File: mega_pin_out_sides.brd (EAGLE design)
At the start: 100 x 85 mm, 102 parts, among them T1 2N2222, T10 2N2222, T11 2N2222, T12 2N2222, T13 2N2222, T14 2N2222, T15 2N2222, T16 2N2222, T17 2N2222, T18 2N2222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

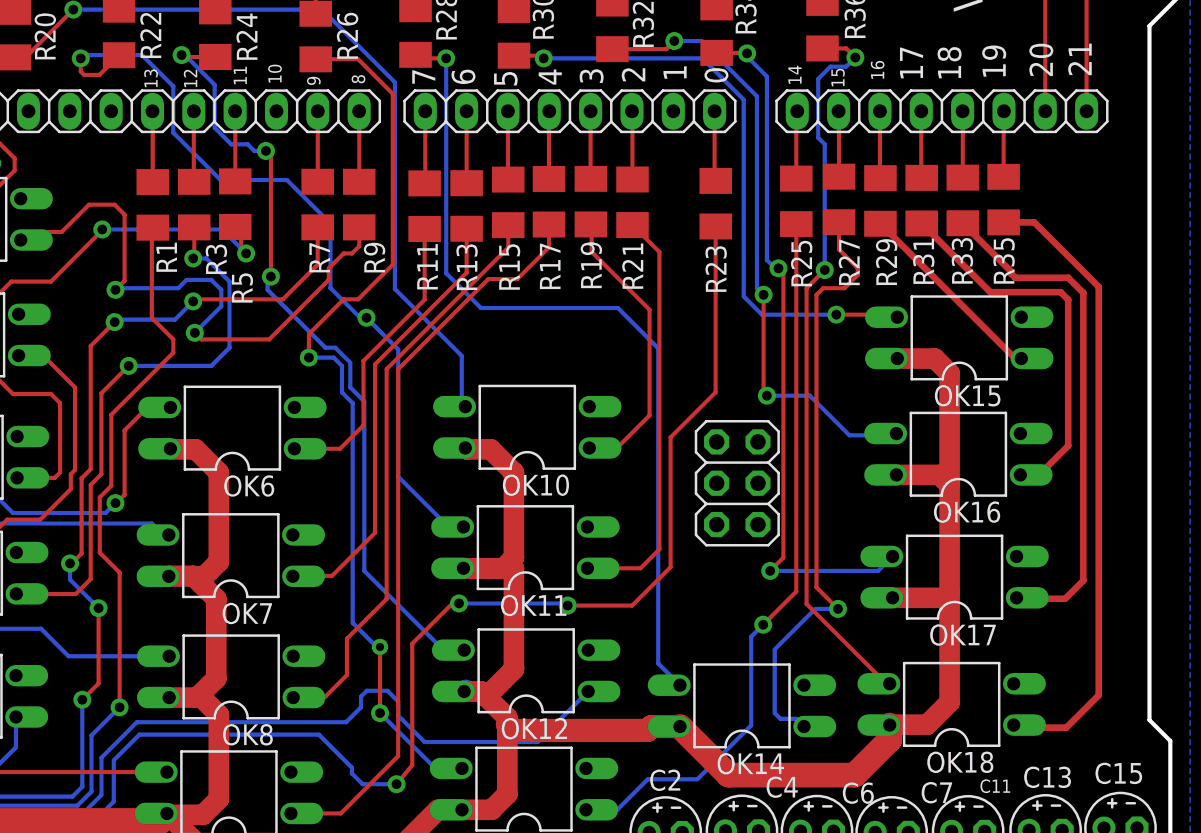
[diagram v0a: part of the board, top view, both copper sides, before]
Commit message: [SIDED] Review and enhancement cont.
- Changed some traces
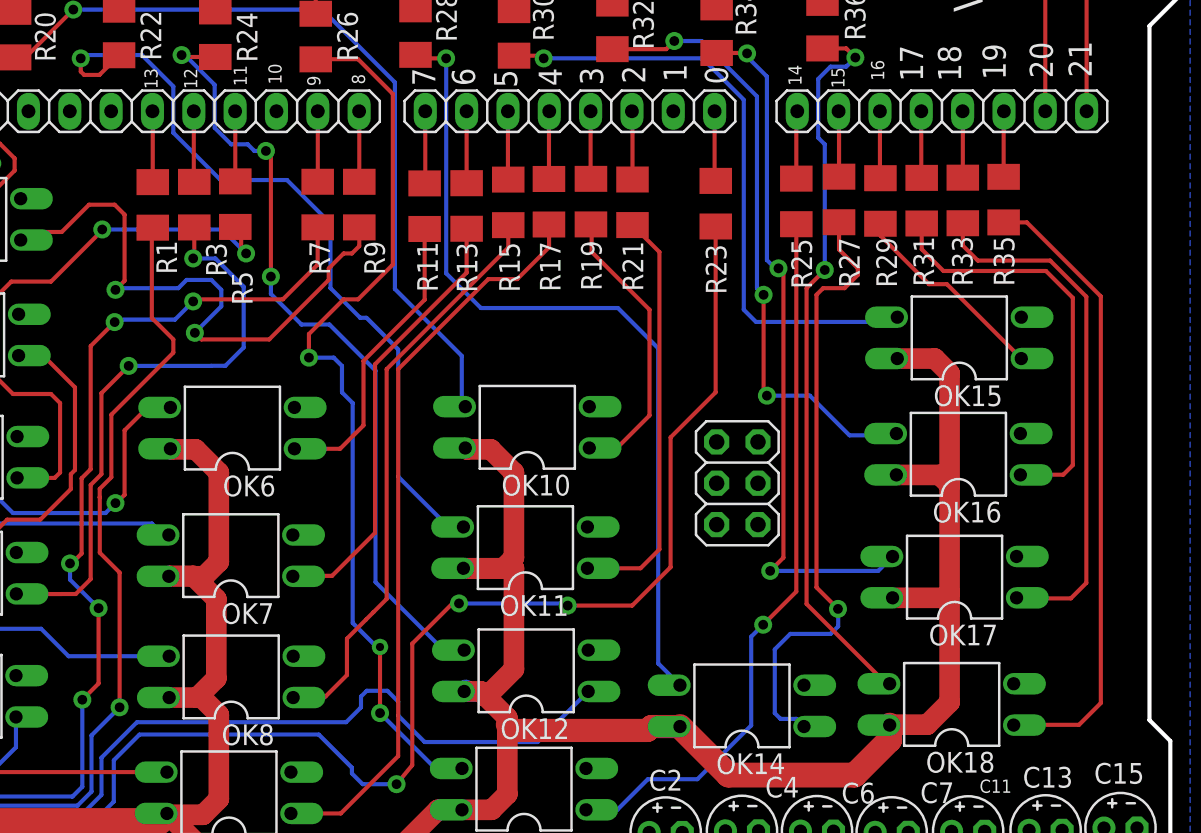
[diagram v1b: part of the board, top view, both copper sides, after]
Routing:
- net N$41: track 23.8 -> 25.9 mm
- net N$5: track 34.6 -> 36.2 mm
- net N$56: track 39.8 -> 38.8 mm
- net N$59: track 31.5 -> 32.6 mm
- net N$50: track 37.6 -> 38.2 mm
- net N$54: track 37.6 -> 38.0 mm, vias 2 -> 1
- net N$39: vias 2 -> 1
